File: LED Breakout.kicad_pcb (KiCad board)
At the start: 2 copper layers, 32.5 x 27.7 mm, 41 parts, among them J1 Conn_02x10_Odd_Even, Q1 MMBT3904, Q2 MMBT3904, Q3 MMBT3904, Q4 MMBT3904, Q5 MMBT3904, Q6 MMBT3904, Q7 MMBT3904, Q8 MMBT3904, SW1 KMR231NG, SW2 KMR231NG, SW3 KMR231NG, SW4 KMR231NG

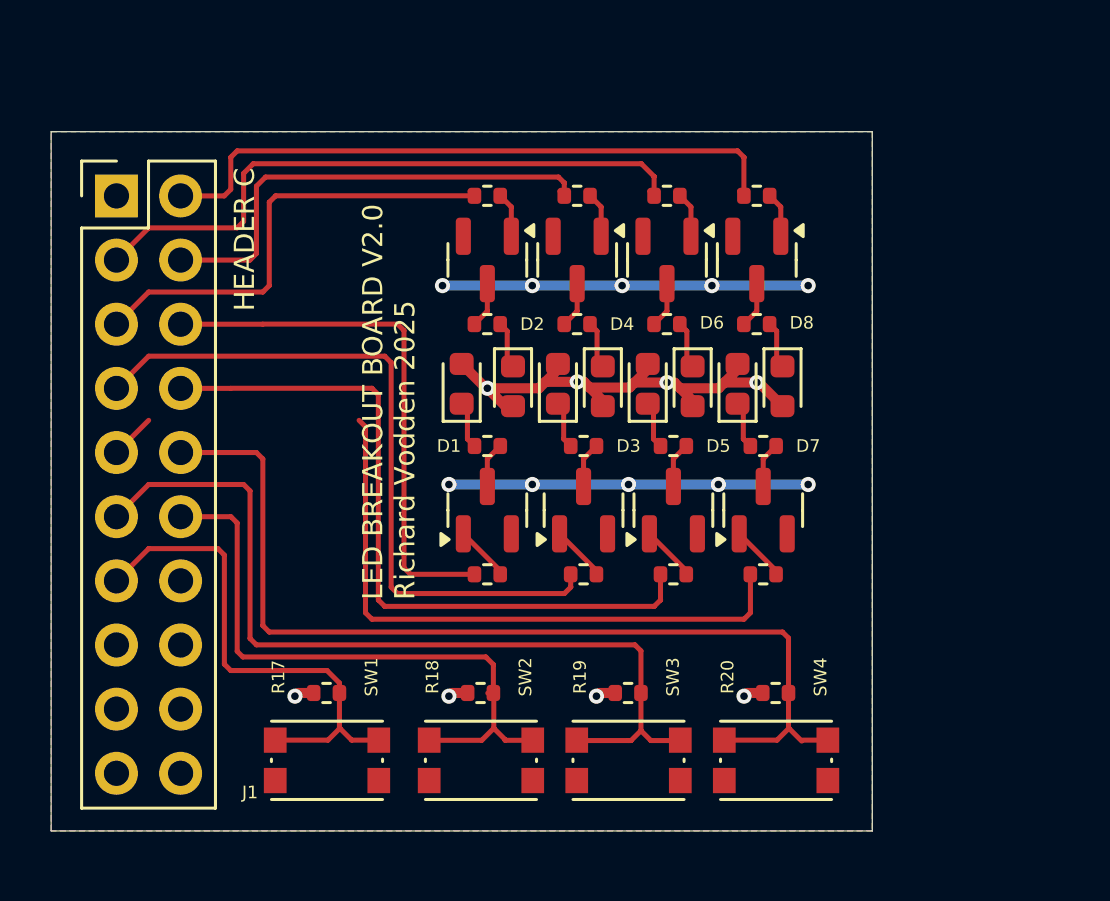
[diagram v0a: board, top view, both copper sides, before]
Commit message: Improved layout to remove symbol warnings
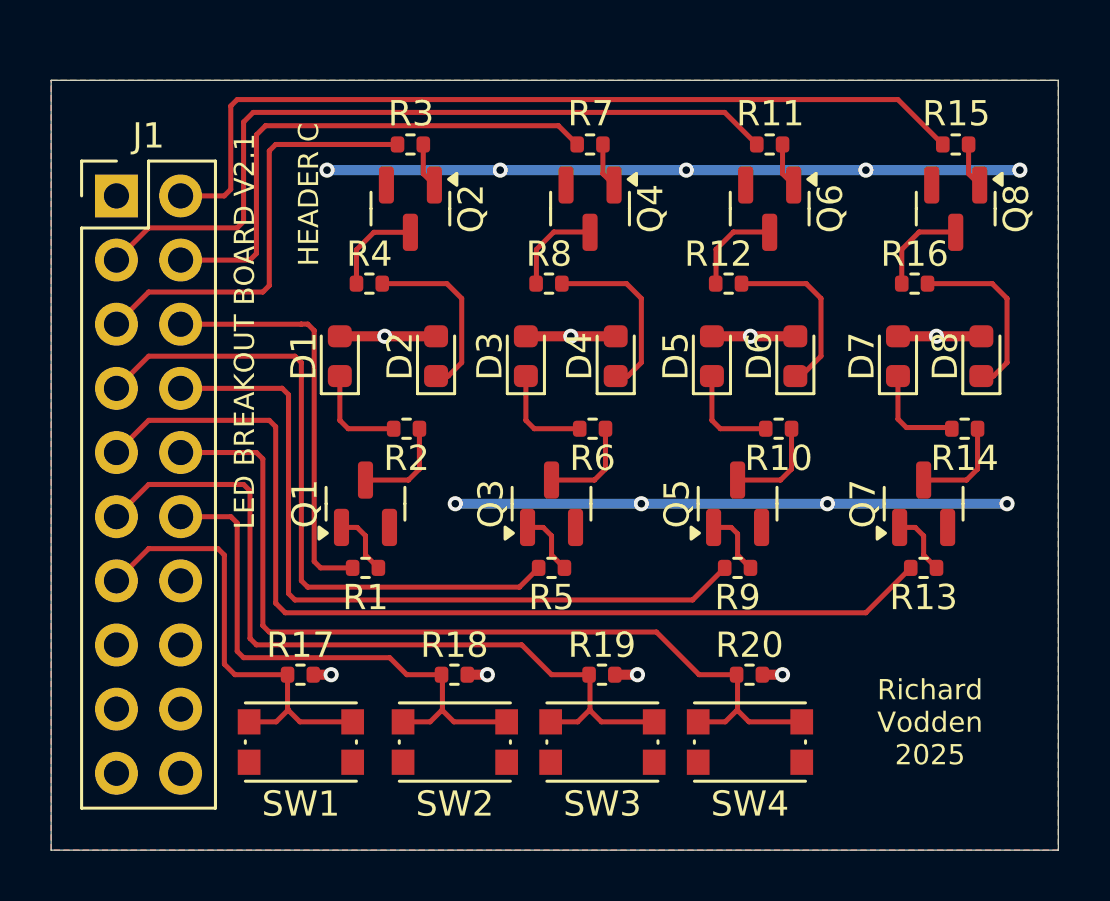
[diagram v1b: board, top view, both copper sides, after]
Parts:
- moved Q8 8.13 mm to (118.4, 42.4)
- moved R15 8.13 mm to (118.4, 39.9), turned to 180 degrees
- moved R14 8.00 mm to (118.7, 51.1)
- moved D8 7.96 mm to (119.4, 48.3), turned to 90 degrees
- moved R16 6.45 mm to (116.7, 45.4)
- moved D7 6.45 mm to (116.1, 48.3)
- moved Q7 6.36 mm to (117.1, 54.1)
- moved R13 6.36 mm to (117.1, 56.6), turned to 180 degrees
- moved D1 4.95 mm to (94.0, 48.3)
- moved R4 4.94 mm to (95.1, 45.4)
- moved Q1 4.83 mm to (95.0, 54.1)
- moved R1 4.83 mm to (95.0, 56.6), turned to 180 degrees
- moved Q6 4.55 mm to (111.0, 42.4)
- moved R11 4.55 mm to (111.0, 39.9), turned to 180 degrees
- moved D6 4.24 mm to (112.0, 48.3), turned to 90 degrees
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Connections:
- R1 pad 1: /IOB_24A -> Net-(Q1-B)
- R1 pad 2: Net-(Q1-B) -> /IOB_24A
- R11 pad 1: /IOB_8A -> Net-(Q6-B)
- R11 pad 2: Net-(Q6-B) -> /IOB_8A
- R13 pad 1: /IOB_5B -> Net-(Q7-B)
- R13 pad 2: Net-(Q7-B) -> /IOB_5B
- R15 pad 1: /IOB_22A -> Net-(Q8-B)
- R15 pad 2: Net-(Q8-B) -> /IOB_22A
- R3 pad 1: /IOB_9B -> Net-(Q2-B)
- R3 pad 2: Net-(Q2-B) -> /IOB_9B
- R5 pad 1: /IOB_4A -> Net-(Q3-B)
- R5 pad 2: Net-(Q3-B) -> /IOB_4A
- R7 pad 1: /IOB_23B -> Net-(Q4-B)
- R7 pad 2: Net-(Q4-B) -> /IOB_23B
- R9 pad 1: /IOB_25B_G3 -> Net-(Q5-B)
- R9 pad 2: Net-(Q5-B) -> /IOB_25B_G3
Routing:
- net GND: track 28.7 -> 49.3 mm, vias 10 -> 9
- net /IOB_5B: track 26.5 -> 40.0 mm
- net /IOB_22A: track 25.8 -> 34.4 mm
- net +3.3V: track 23.1 -> 16.8 mm
- net Net-(D4-K): track 1.54 -> 7.17 mm
- net Net-(D8-K): track 1.54 -> 7.17 mm
- net Net-(D2-K): track 1.54 -> 7.17 mm
- net Net-(D6-K): track 1.54 -> 7.02 mm
- net /IOB_8A: track 25.4 -> 30.6 mm
- net /IOB_24A: track 21.2 -> 16.2 mm
- net /IOB_29B: track 39.1 -> 35.3 mm
- net /IOB_2A: track 35.0 -> 31.6 mm
- net /IOB_31B: track 25.0 -> 21.8 mm
- net /IOB_3B_G6: track 20.4 -> 17.8 mm
- net Net-(D7-K): track 1.54 -> 4.02 mm
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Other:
- board size 32.5 x 27.7 mm -> 39.9 x 30.5 mm
- board text added: "LED BREAKOUT BOARD V2.1"
- board text removed: "LED BREAKOUT BOARD V2.0"
